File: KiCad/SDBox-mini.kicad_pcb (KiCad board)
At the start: 2 copper layers, 36.1 x 34 mm, 28 parts, among them J1 DB25_Male, J2 Conn_02x03_Odd_Even, J3 Micro_SD_Card, J4 USB_B_Micro, U1 LM1117-3.3, U2 ATmega328P-AU, U3 74LVC3G17, U4 74LVC1G17, Y1 Crystal_GND24_Small

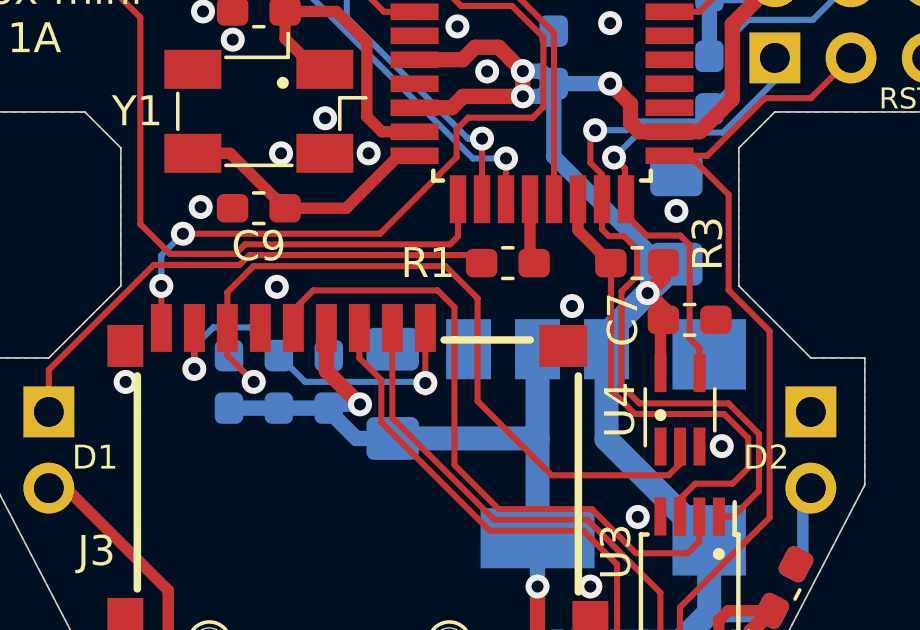
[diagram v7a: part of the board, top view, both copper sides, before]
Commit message: added a 10k resistor pack and set individual pull-ups for DAT1,DAT2-lines (pin 8,1)
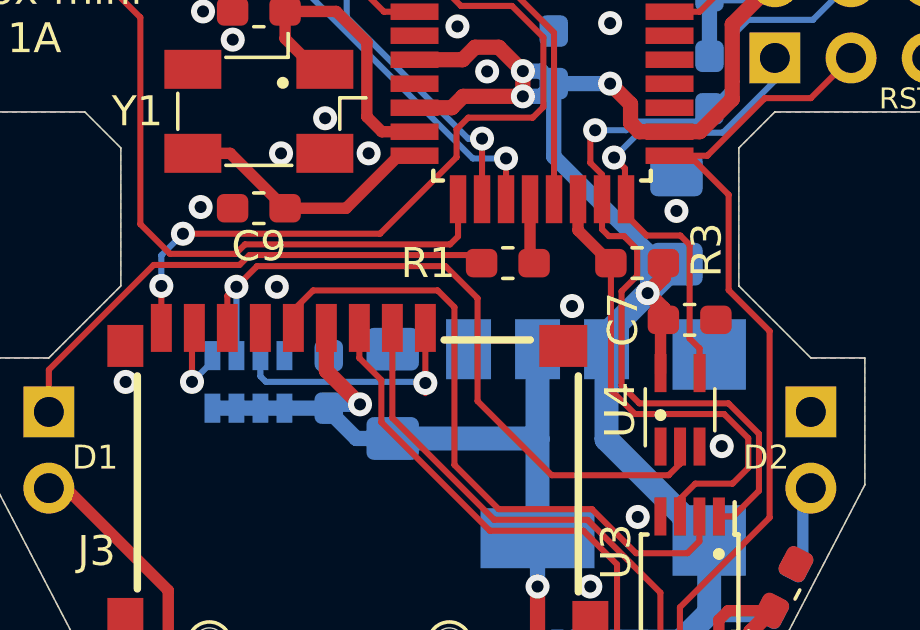
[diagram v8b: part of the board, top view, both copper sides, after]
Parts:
- removed the R4 at (99.8, 70.5)
- removed the R5 at (101.5, 70.5)
- added RN1: 10k, SDBox-mini:RESCAF80P320X160X60-8N, B.Cu at (100.5, 70.5)
- renumbered R6 to R4, R7 to R5
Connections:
- J3 pad 1: Net-(J3-Pad1) -> DAT2
- J3 pad 8: Net-(J3-Pad1) -> DAT1
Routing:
- net Net-(J3-Pad1): track 13.0 -> 0.00 mm, vias 2 -> 0
- net DAT2: track 0.00 -> 8.45 mm, vias 0 -> 1
- net DAT1: track 0.00 -> 2.99 mm, vias 0 -> 1
- net MISO_3V3: track 25.6 -> 24.5 mm
- net 3V3: track 38.3 -> 39.3 mm
